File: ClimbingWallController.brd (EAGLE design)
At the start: 100 x 80 mm, 339 parts, among them IC1 74HCT138D, IC2 SN74LV4052AD, IC3 PIC24FJ32GB004, IC4 TLC5952, IC5 TLC5952, IC6 TC1015, IC8 74HCT138D, IC9 SN74LV4052AD, J1 PWR, Q1 DPBT8105, Q10 DPBT8105, Q11 DPBT8105, Q12 DPBT8105, Q13 DPBT8105, Q14 DPBT8105, Q15 DPBT8105, Q16 DPBT8105, Q17 DPBT8105, Q2 DPBT8105, Q3 DPBT8105, Q4 DPBT8105, Q5 DPBT8105, Q6 DPBT8105, Q7 DPBT8105, Q8 DPBT8105, Q9 NC, X1 MINI-USB-32005-201

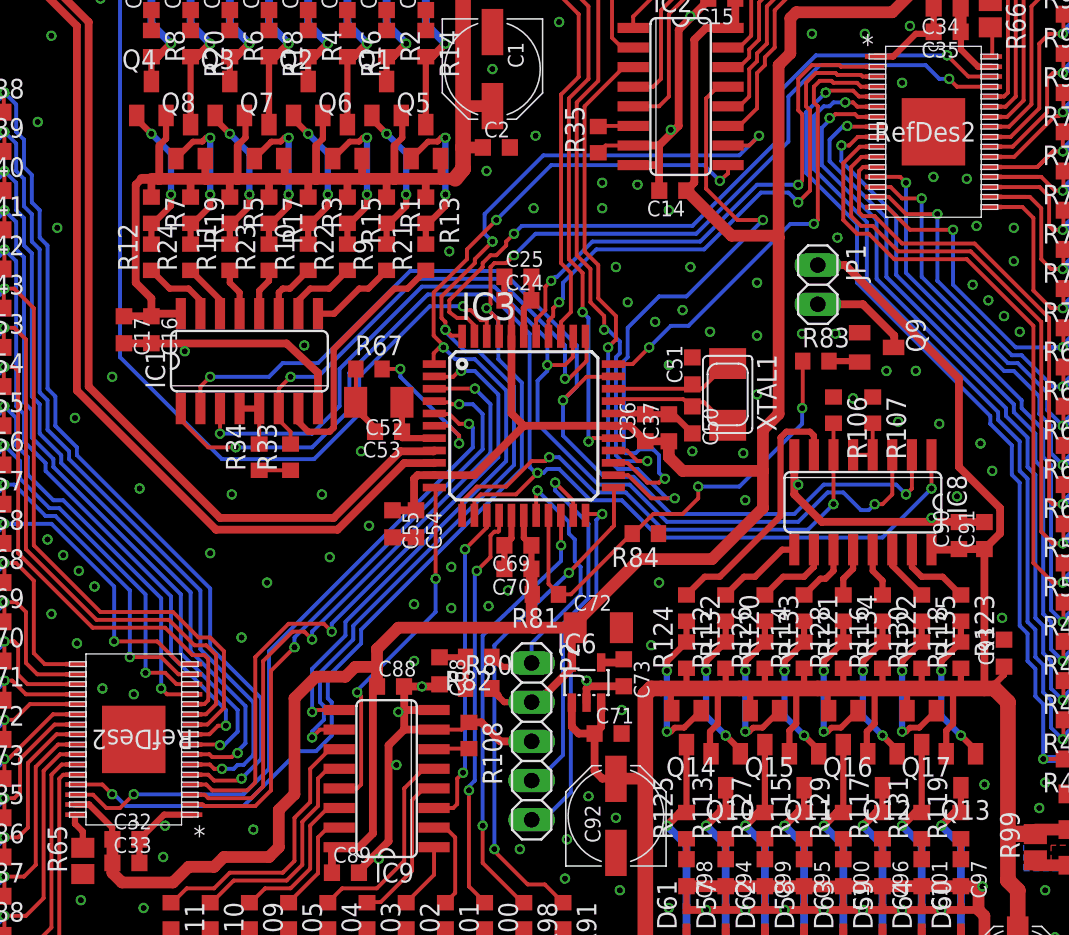
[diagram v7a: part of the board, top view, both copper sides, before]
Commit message: Increased LED Driver power pad to recommended specs. Exported BOM, massaged, and identified parts at digikey.csv. Setup a Digikey BOM.
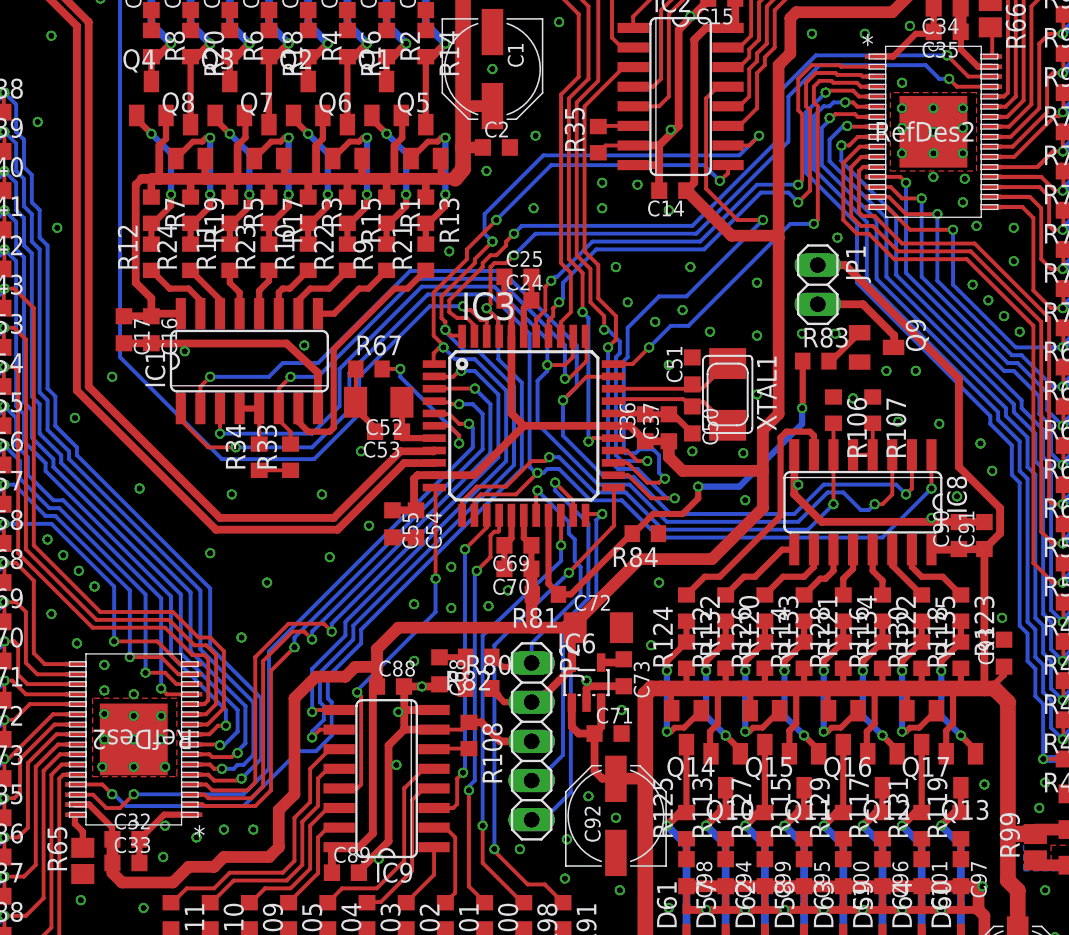
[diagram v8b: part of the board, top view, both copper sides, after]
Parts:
- Q9: device transistor:SOT23-EBC -> transistor:SOT23-BEC
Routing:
- net N$50: track 2.01 -> 2.75 mm
- net GND: vias 225 -> 247
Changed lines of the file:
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@@
 <layer number="27" name="tValues" color="7" fill="1" visible="no" active="yes"/>
 <layer number="28" name="bValues" color="7" fill="1" visible="no" active="yes"/>
-<layer number="29" name="tStop" color="7" fill="3" visible="no" active="yes"/>
-<layer number="30" name="bStop" color="7" fill="6" visible="no" active="yes"/>
-<layer number="31" name="tCream" color="7" fill="4" visible="no" active="yes"/>
-<layer number="32" name="bCream" color="7" fill="5" visible="no" active="yes"/>
+<layer number="29" name="tStop" color="7" fill="3" visible="yes" active="yes"/>
+<layer number="30" name="bStop" color="7" fill="6" visible="yes" active="yes"/>
+<layer number="31" name="tCream" color="7" fill="4" visible="yes" active="yes"/>
+<layer number="32" name="bCream" color="7" fill="5" visible="yes" active="yes"/>
 <layer number="33" name="tFinish" color="6" fill="3" visible="yes" active="yes"/>
 <layer number="34" name="bFinish" color="6" fill="6" visible="yes" active="yes"/>
@@
 <element name="R81" library="Parts" package="R0603" value="NC" x="50.927" y="29.718" rot="R180"/>
 <element name="R84" library="Parts" package="R0603" value="NC" x="57.404" y="33.655" rot="R180"/>
-<element name="Q9" library="transistor" package="SOT23-EBC" value="NC" x="72.39" y="45.72" rot="R270"/>
 <element name="R83" library="Parts" package="R0603" value="NC" x="68.453" y="44.831"/>
 <element name="C14" library="rcl" package="C0603K" value="0.1uF" x="59.182" y="55.88" rot="R180"/>
@@
 <attribute name="MF" value="" x="88.392" y="14.478" size="1.778" layer="27" rot="R270" display="off"/>
 </element>
+<element name="Q9" library="transistor" package="SOT23-BEC" value="NC" x="72.39" y="45.72" rot="R270"/>
 </elements>
 <signals>
@@
 <contactref element="C71" pad="2"/>
 <contactref element="R84" pad="1"/>
-<contactref element="Q9" pad="E"/>
 <contactref element="C14" pad="2"/>
 <contactref element="C88" pad="2"/>
@@
 <via x="81.28" y="53.467" extent="1-16" drill="0.381"/>
 <via x="81.28" y="51.308" extent="1-16" drill="0.381"/>
-<via x="78.232" y="56.642" extent="1-16" drill="0.381"/>
+<via x="78.105" y="56.642" extent="1-16" drill="0.381"/>
 <via x="39.497" y="34.163" extent="1-16" drill="0.381"/>
 <via x="78.867" y="53.594" extent="1-16" drill="0.381"/>
@@
 <via x="18.923" y="28.448" extent="1-16" drill="0.381"/>
 <via x="24.257" y="23.241" extent="1-16" drill="0.381"/>
-<via x="22.225" y="23.622" extent="1-16" drill="0.381"/>
+<via x="22.352" y="25.146" extent="1-16" drill="0.381"/>
 <via x="20.574" y="26.543" extent="1-16" drill="0.381"/>
 <via x="60.325" y="67.183" extent="1-16" drill="0.381"/>
@@
 <contactref element="IC7" pad="1"/>
 <via x="98.679" y="6.731" extent="1-16" drill="0.381"/>
+<contactref element="Q9" pad="E"/>
+<polygon width="0.254" layer="1" isolate="0.254" thermals="no">
+<vertex x="73.279" y="62.23"/>
+<vertex x="73.279" y="57.15"/>
+<vertex x="78.867" y="57.15"/>
+<vertex x="78.867" y="62.23"/>
+</polygon>
+<via x="74.041" y="61.214" extent="1-16" drill="0.381"/>
+<via x="74.041" y="59.944" extent="1-16" drill="0.381"/>
+<via x="74.041" y="58.293" extent="1-16" drill="0.381"/>
+<via x="76.073" y="58.293" extent="1-16" drill="0.381"/>
+<via x="77.978" y="58.293" extent="1-16" drill="0.381"/>
+<via x="77.978" y="59.944" extent="1-16" drill="0.381"/>
+<via x="76.073" y="61.214" extent="1-16" drill="0.381"/>
+<via x="77.978" y="61.214" extent="1-16" drill="0.381"/>
+<via x="76.073" y="59.69" extent="1-16" drill="0.381"/>
+<polygon width="0.254" layer="1" isolate="0.254" thermals="no">
+<vertex x="21.59" y="22.987"/>
+<vertex x="21.59" y="17.907"/>
+<vertex x="27.051" y="17.907"/>
+<vertex x="27.051" y="18.034"/>
+<vertex x="27.051" y="22.987"/>
+</polygon>
+<via x="22.225" y="18.542" extent="1-16" drill="0.381"/>
+<via x="26.289" y="18.542" extent="1-16" drill="0.381"/>
+<via x="24.257" y="18.542" extent="1-16" drill="0.381"/>
+<via x="24.257" y="20.32" extent="1-16" drill="0.381"/>
+<via x="26.035" y="20.32" extent="1-16" drill="0.381"/>
+<via x="22.352" y="20.32" extent="1-16" drill="0.381"/>
+<via x="22.352" y="21.971" extent="1-16" drill="0.381"/>
+<via x="22.352" y="23.495" extent="1-16" drill="0.381"/>
+<via x="24.257" y="21.844" extent="1-16" drill="0.381"/>
+<via x="26.035" y="21.844" extent="1-16" drill="0.381"/>
+<via x="28.321" y="13.97" extent="1-16" drill="0.381"/>
+<via x="30.099" y="14.478" extent="1-16" drill="0.381"/>
+<via x="77.978" y="55.118" extent="1-16" drill="0.381"/>
 </signal>
 <signal name="ROW0">
@@
 <contactref element="IC3" pad="19"/>
 <contactref element="R83" pad="1"/>
-<wire x1="67.603" y1="44.831" x2="67.603" y2="41.822" width="0.254" layer="1"/>
+<wire x1="67.603" y1="44.831" x2="67.603" y2="41.822" width="0.4064" layer="1"/>
 <wire x1="67.603" y1="41.822" x2="67.564" y2="41.783" width="0.254" layer="1"/>
 <via x="67.564" y="41.783" extent="1-16" drill="0.381"/>
-<wire x1="67.564" y1="41.783" x2="67.564" y2="40.767" width="0.254" layer="16"/>
+<wire x1="67.564" y1="41.783" x2="67.564" y2="40.767" width="0.4064" layer="16"/>
 <via x="60.833" y="36.703" extent="1-16" drill="0.381"/>
-<wire x1="51.13" y1="34.84" x2="51.13" y2="30.404" width="0.254" layer="1"/>
-<wire x1="51.13" y1="30.404" x2="51.816" y2="29.718" width="0.254" layer="1"/>
-<wire x1="51.816" y1="29.718" x2="52.578" y2="29.718" width="0.254" layer="1"/>
-<wire x1="52.578" y1="29.718" x2="56.515" y2="33.655" width="0.254" layer="1"/>
+<wire x1="51.13" y1="34.84" x2="51.13" y2="30.404" width="0.4064" layer="1"/>
+<wire x1="51.13" y1="30.404" x2="51.816" y2="29.718" width="0.4064" layer="1"/>
+<wire x1="51.816" y1="29.718" x2="52.578" y2="29.718" width="0.4064" layer="1"/>
+<wire x1="52.578" y1="29.718" x2="56.515" y2="33.655" width="0.4064" layer="1"/>
 <wire x1="56.554" y1="33.655" x2="56.642" y2="33.655" width="0.254" layer="1"/>
-<wire x1="56.642" y1="33.655" x2="57.912" y2="34.925" width="0.254" layer="1"/>
+<wire x1="56.642" y1="33.655" x2="57.912" y2="34.925" width="0.4064" layer="1"/>
 <contactref element="R84" pad="2"/>
 <contactref element="R81" pad="1"/>
-<wire x1="57.912" y1="34.925" x2="59.817" y2="34.925" width="0.254" layer="1"/>
-<wire x1="59.817" y1="34.925" x2="60.833" y2="35.941" width="0.254" layer="1"/>
-<wire x1="60.833" y1="35.941" x2="60.833" y2="36.703" width="0.254" layer="1"/>
-<wire x1="67.564" y1="40.767" x2="63.5" y2="36.703" width="0.254" layer="16"/>
-<wire x1="63.5" y1="36.703" x2="60.833" y2="36.703" width="0.254" layer="16"/>
+<wire x1="57.912" y1="34.925" x2="59.817" y2="34.925" width="0.4064" layer="1"/>
+<wire x1="59.817" y1="34.925" x2="60.833" y2="35.941" width="0.4064" layer="1"/>
+<wire x1="60.833" y1="35.941" x2="60.833" y2="36.703" width="0.4064" layer="1"/>
+<wire x1="67.564" y1="40.767" x2="63.5" y2="36.703" width="0.4064" layer="16"/>
+<wire x1="63.5" y1="36.703" x2="60.833" y2="36.703" width="0.4064" layer="16"/>
 <wire x1="56.554" y1="33.655" x2="56.515" y2="33.655" width="0.254" layer="1"/>
 <wire x1="51.816" y1="29.718" x2="51.777" y2="29.718" width="0.254" layer="1"/>
@@
 <wire x1="90.9078" y1="11.1518" x2="91.694" y2="11.176" width="0.762" layer="1"/>
 </signal>
-<signal name="N$87">
-<contactref element="Q9" pad="B"/>
-<contactref element="R83" pad="2"/>
-<wire x1="69.303" y1="44.831" x2="71.229" y2="44.831" width="0.4064" layer="1"/>
-<wire x1="71.229" y1="44.831" x2="71.29" y2="44.77" width="0.4064" layer="1"/>
-</signal>
 <signal name="N$88">
-<contactref element="Q9" pad="C"/>
 <contactref element="JP1" pad="2"/>
 <wire x1="68.58" y1="48.514" x2="71.501" y2="48.514" width="0.508" layer="1"/>
 <wire x1="71.501" y1="48.514" x2="73.533" y2="46.482" width="0.508" layer="1"/>
 <wire x1="73.533" y1="46.482" x2="73.533" y2="45.763" width="0.508" layer="1"/>
-<wire x1="73.533" y1="45.763" x2="73.49" y2="45.72" width="0.508" layer="1"/>
+<contactref element="Q9" pad="C"/>
+<wire x1="73.49" y1="45.72" x2="73.533" y2="45.763" width="0" layer="19" extent="1-1"/>
 </signal>
 <signal name="N$89">
@@
 <wire x1="71.374" y1="72.097" x2="71.374" y2="76.327" width="0.4064" layer="1"/>
 </signal>
+<signal name="N$50">
+<contactref element="R83" pad="2"/>
+<contactref element="Q9" pad="B"/>
+<wire x1="69.303" y1="44.831" x2="69.451" y2="44.831" width="0.4064" layer="1"/>
+<wire x1="69.451" y1="44.831" x2="71.29" y2="46.67" width="0.4064" layer="1"/>
+</signal>
 </signals>
